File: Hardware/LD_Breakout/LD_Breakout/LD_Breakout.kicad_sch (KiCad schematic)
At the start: 5 parts

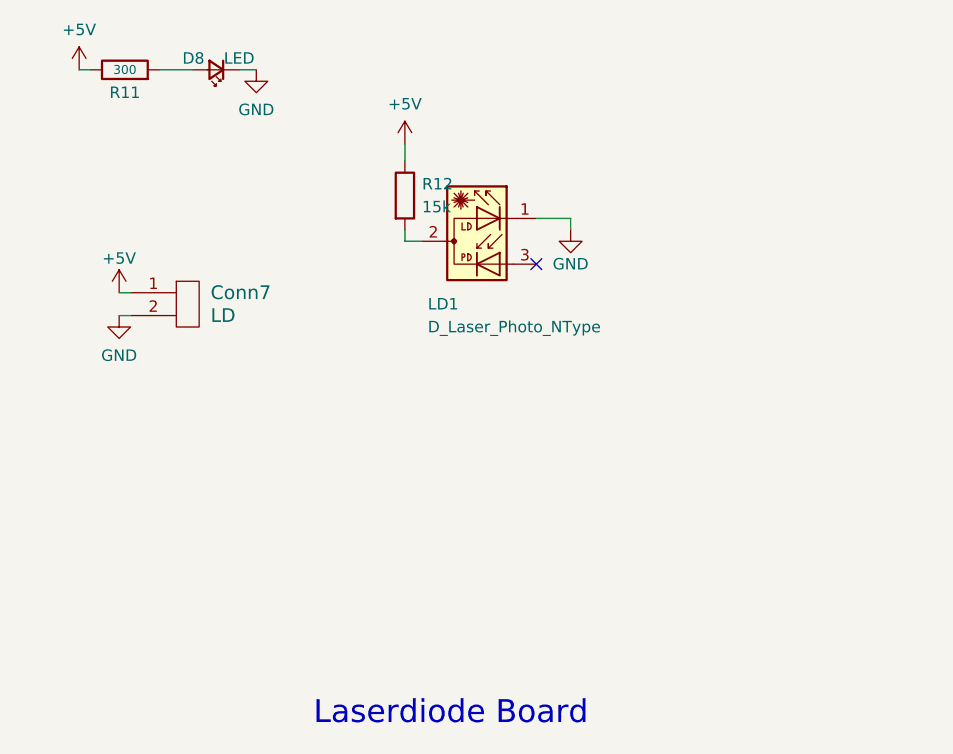
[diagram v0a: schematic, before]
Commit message: Separated Layouts
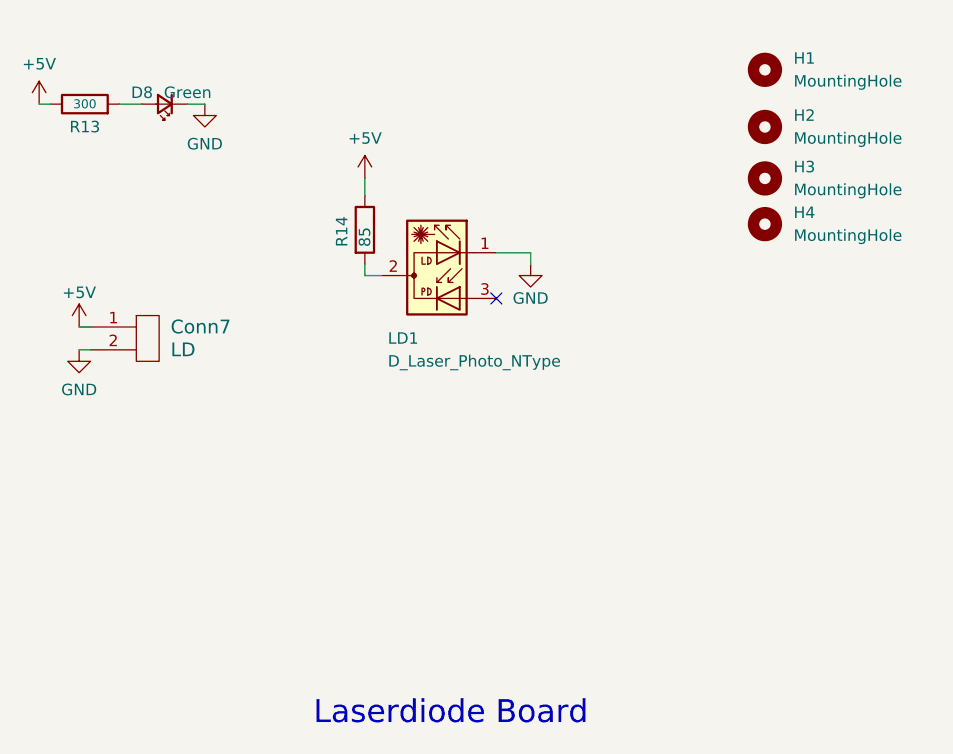
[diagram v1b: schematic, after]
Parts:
- removed R11: 300, Resistor_SMD:R_0603_1608Metric_Pad0.98x0.95mm_HandSolder, symbol Device:R
- removed R12: 15k, symbol Device:R
- added H1, H2, H3, H4: MountingHole, MRDT_Drill_Holes:4_40_Hole_Corner, symbol Mechanical:MountingHole
- added R13: 300, Resistor_SMD:R_0603_1608Metric_Pad0.98x0.95mm_HandSolder, symbol Device:R
- added R14: 85, LED_SMD:LED_0603_1608Metric_Pad1.05x0.95mm_HandSolder, symbol Device:R
- Conn7: footprint (none) -> MRDT_Connectors:MOLEX_SL_02_Vertical
- D8: value LED -> Green
- LD1: footprint (none) -> FTIR_Footprints:RLD63NPC5
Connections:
- net +5V: now also R13.1, R14.1
- net at D8.2 (A): now also R13.2
- net at LD1.2: now also R14.2
